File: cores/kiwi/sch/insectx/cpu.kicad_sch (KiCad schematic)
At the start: 31 parts, among them U11 74LS04, U12 74LS08, U13 74LS74, U14 74LS74, U15 74LS174, U17 74LS74, U18 74LS157, U19 74LS157, U20 74LS157, U21 74LS157, U25 PAL16L8, U26 PAL16L8, U27 74LS245, U28 74LS245, U30 HM6264, U31 uPD43256BCZ-B, U32 27C010, U34 Z80CPU, U35 PAL16L8, U36 PAL16L8, U37 74LS174, U38 27512, U39 Z80CPU

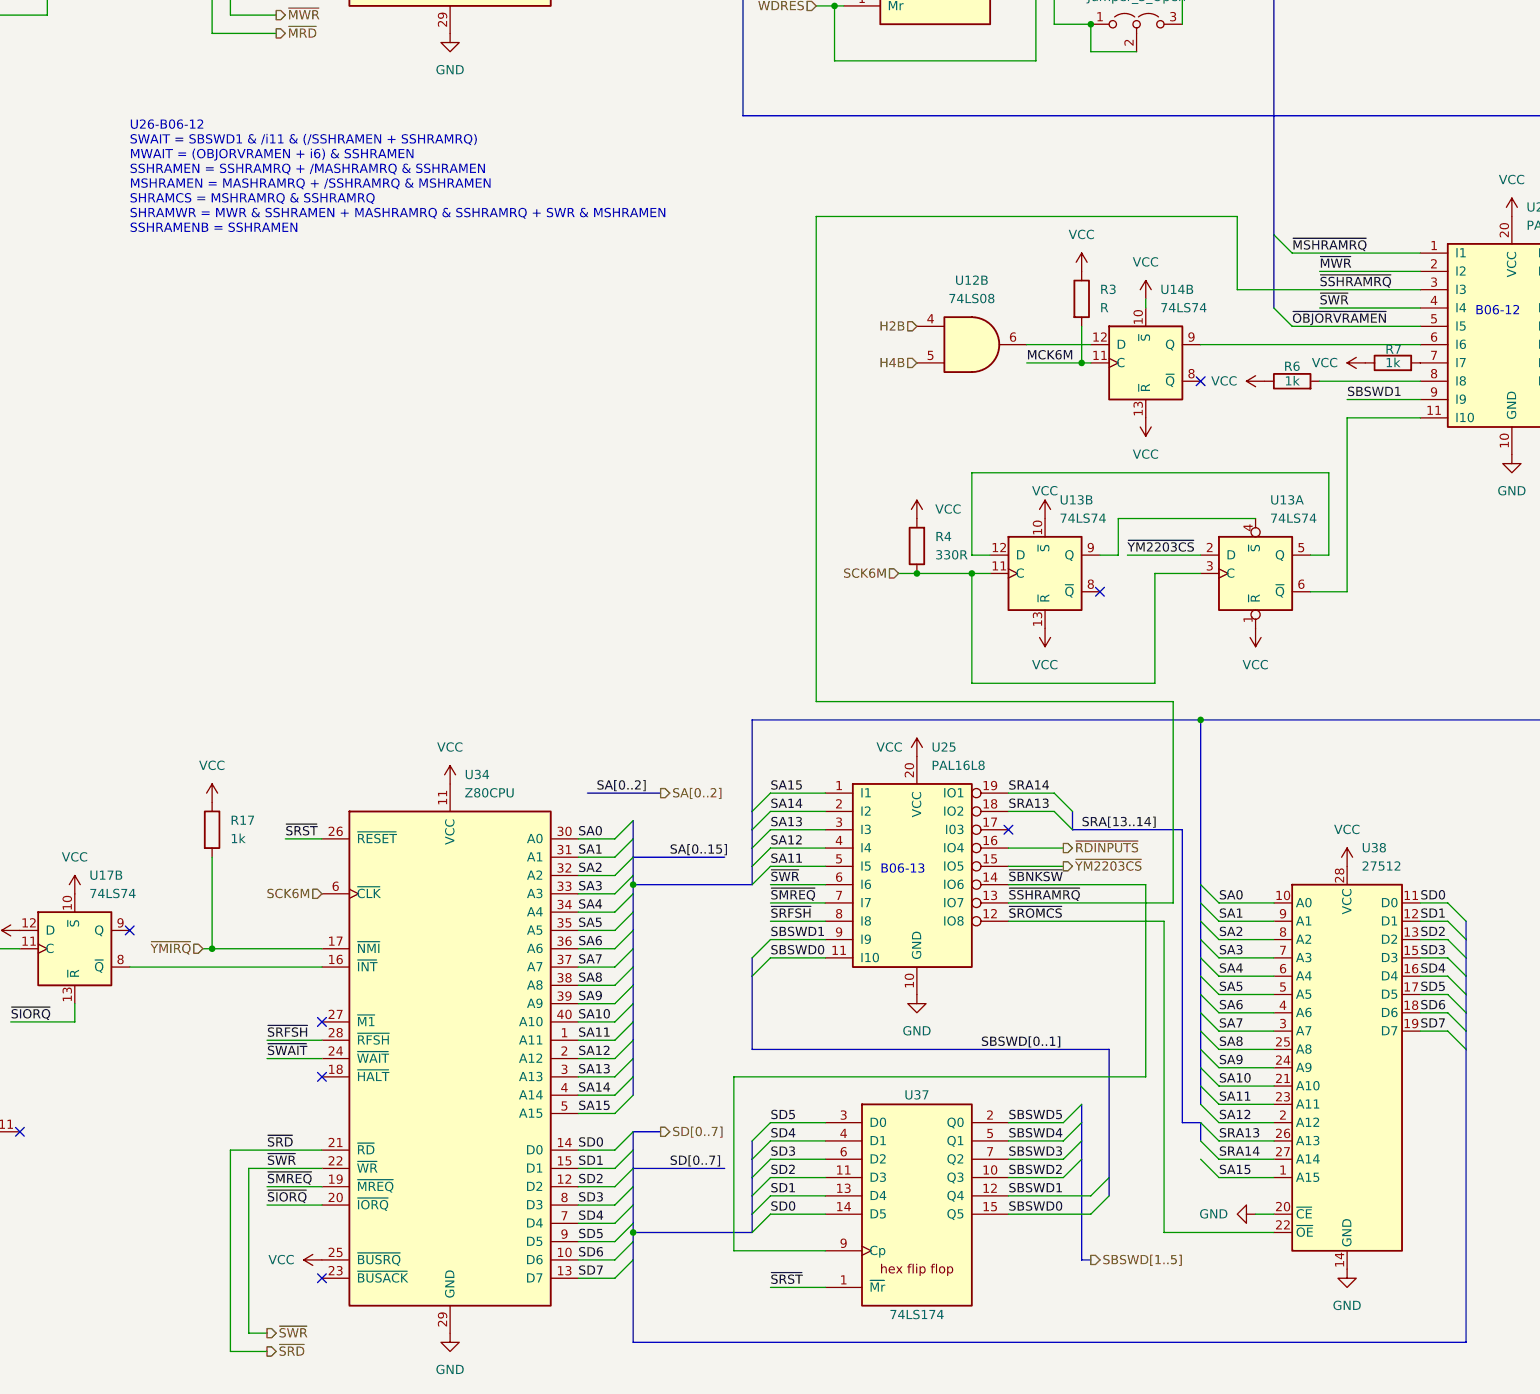
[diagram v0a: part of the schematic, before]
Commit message: Updated schematics according to: [insectx] schematic signals #22
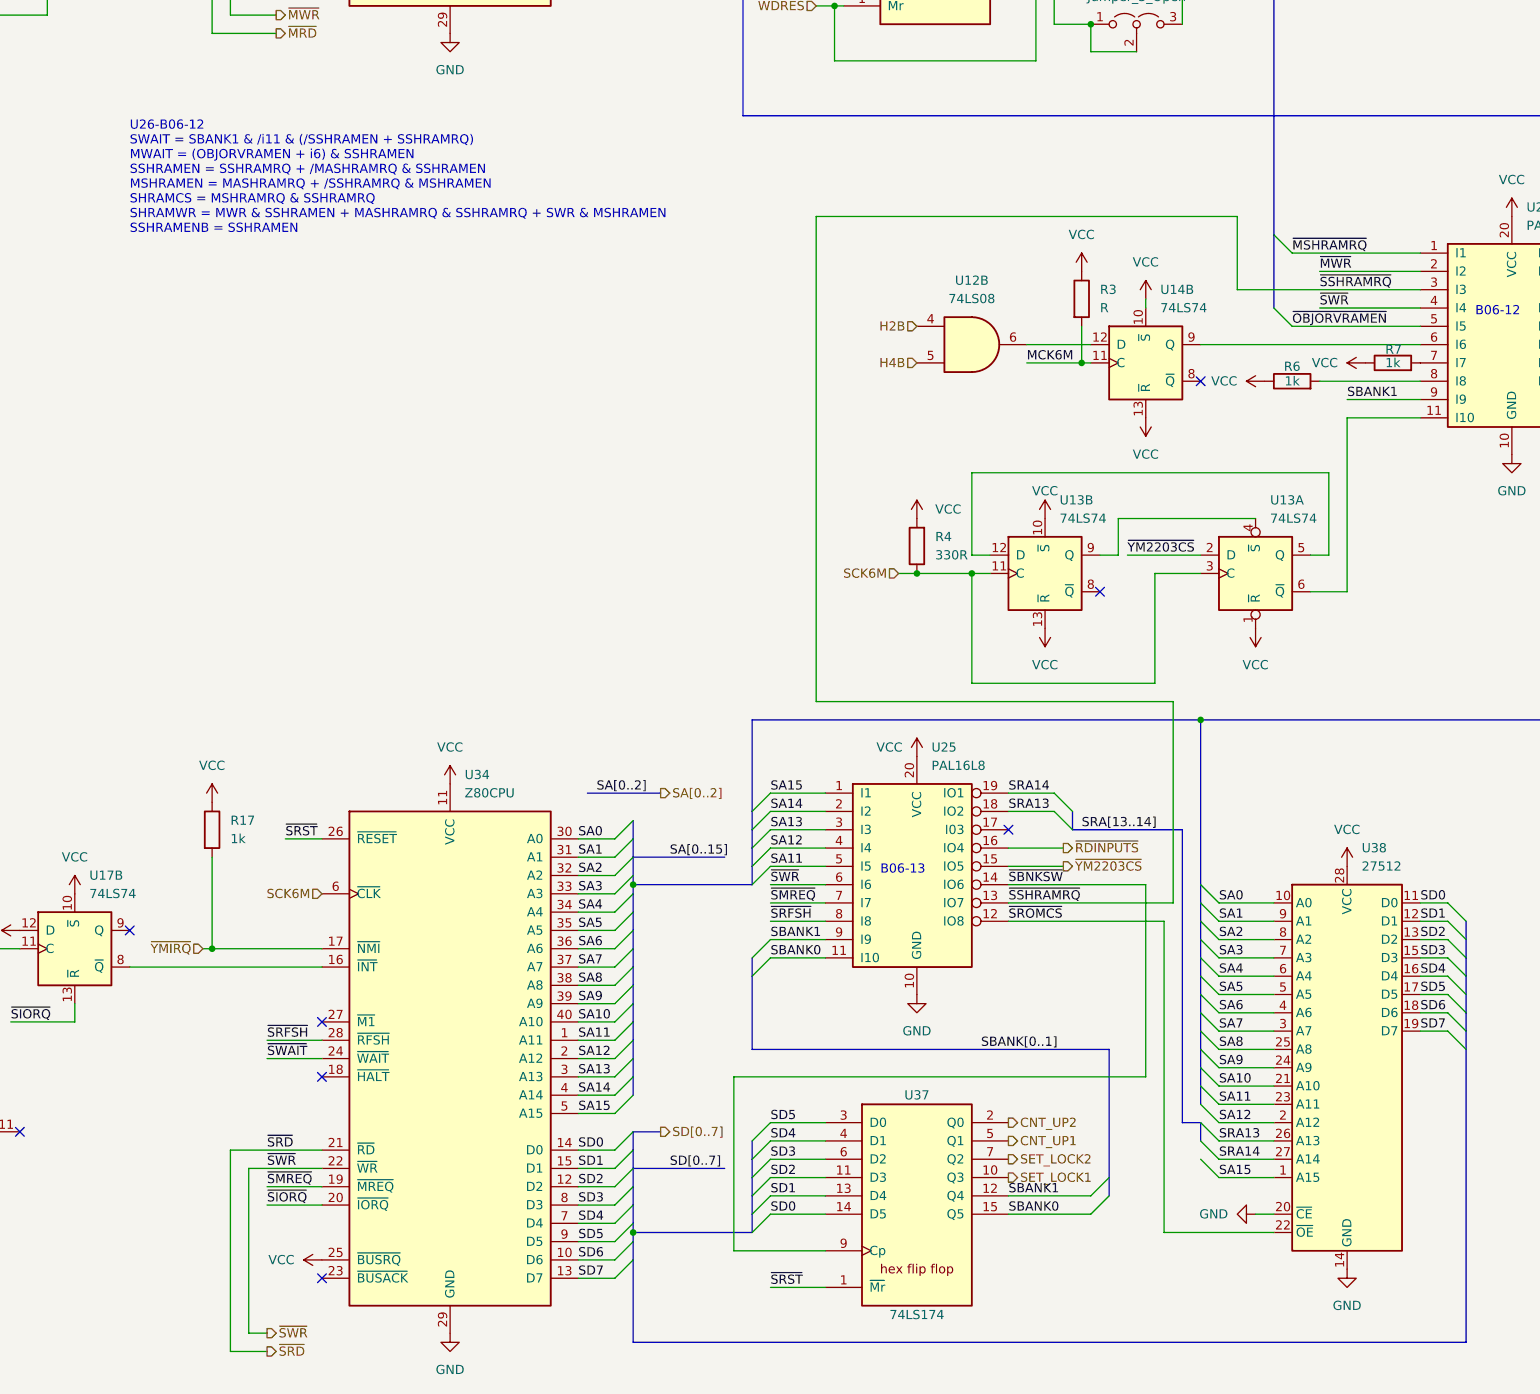
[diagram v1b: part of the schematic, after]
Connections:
- net SBSWD0 renamed SBANK0
- net SBSWD1 renamed SBANK1
- net SBSWD2 renamed SET_LOCK1
- net SBSWD3 renamed SET_LOCK2
- net SBSWD4 renamed CNT_UP1
- net SBSWD5 renamed CNT_UP2
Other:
- note added: "U26-B06-12 SWAIT = SBANK1 & /i11 & (/SSHRAMEN + SSHRAMRQ) MWAIT = (OBJORVRAMEN + i6) & SSHRAMEN SSHRAMEN = SSHRAMRQ + /MASHRAMRQ & SSHRAMEN MSHRAMEN = MASHRAMRQ + /SSHRAMRQ & MSHRAMEN SHRAMCS = MSHRAMRQ & SSHRAMRQ SHRAMWR = MWR & SSHRAMEN + MASHRAMRQ & SSHRAMRQ + SWR & MSHRAMEN SSHRAMENB = SSHRAMEN"
- note removed: "U26-B06-12 SWAIT = SBSWD1 & /i11 & (/SSHRAMEN + SSHRAMRQ) MWAIT = (OBJORVRAMEN + i6) & SSHRAMEN SSHRAMEN = SSHRAMRQ + /MASHRAMRQ & SSHRAMEN MSHRAMEN = MASHRAMRQ + /SSHRAMRQ & MSHRAMEN SHRAMCS = MSHRAMRQ & SSHRAMRQ SHRAMWR = MWR & SSHRAMEN + MASHRAMRQ & SSHRAMRQ + SWR & MSHRAMEN SSHRAMENB = SSHRAMEN"
